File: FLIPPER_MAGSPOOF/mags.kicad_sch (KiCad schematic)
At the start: 7 parts, among them J2 Conn_01x10_Socket, J3 Coil, J3 Conn_01x08_Socket, J4 Conn_01x08_Socket, J5 Conn_01x10_Socket, SW1 On, U3 TC4424

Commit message: BOM updated
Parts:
- J2: LCSC# C492418 -> C57369; manf# PZ254R-11-10P -> (none)
- J3: LCSC# C2894950 -> C492407; manf# PZ254-1-08-W-8.5 -> (none)
- J4: LCSC# C2894950 -> C492407; manf# PZ254-1-08-W-8.5 -> (none); now not fitted
- J5: LCSC# C492418 -> C57369; manf# PZ254R-11-10P -> (none); now not fitted
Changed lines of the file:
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@@
       (effects (font (size 1.27 1.27)) hide)
     )
-    (property "manf#" "PZ254-1-08-W-8.5" (at 116.713 36.068 0)
-      (effects (font (size 1.27 1.27)) hide)
-    )
-    (property "LCSC#" "C2894950" (at 116.713 36.068 0)
+    (property "manf#" "" (at 116.713 36.068 0)
+      (effects (font (size 1.27 1.27)) hide)
+    )
+    (property "LCSC#" "C492407" (at 116.713 36.068 0)
       (effects (font (size 1.27 1.27)) hide)
     )
@@
   )
   (symbol (lib_id "Connector:Conn_01x08_Socket") (at 141.2748 37.3126 0) (unit 1)
-    (in_bom yes) (on_board yes) (dnp no)
+    (in_bom yes) (on_board yes) (dnp yes)
     (property "Reference" "J4" (at 139.3698 26.7716 0)
       (effects (font (size 1.27 1.27)) (justify left))
@@
       (effects (font (size 1.27 1.27)) hide)
     )
-    (property "manf#" "PZ254-1-08-W-8.5" (at 141.2748 37.3126 0)
-      (effects (font (size 1.27 1.27)) hide)
-    )
-    (property "LCSC#" "C2894950" (at 141.2748 37.3126 0)
+    (property "manf#" "" (at 141.2748 37.3126 0)
+      (effects (font (size 1.27 1.27)) hide)
+    )
+    (property "LCSC#" "C492407" (at 141.2748 37.3126 0)
       (effects (font (size 1.27 1.27)) hide)
     )
@@
   )
   (symbol (lib_id "Connector:Conn_01x10_Socket") (at 142.5702 72.2376 0) (unit 1)
-    (in_bom yes) (on_board yes) (dnp no)
+    (in_bom yes) (on_board yes) (dnp yes)
     (property "Reference" "J5" (at 141.4272 60.0456 0)
       (effects (font (size 1.27 1.27)) (justify left))
@@
       (effects (font (size 1.27 1.27)) hide)
     )
-    (property "manf#" "PZ254R-11-10P" (at 142.5702 72.2376 0)
-      (effects (font (size 1.27 1.27)) hide)
-    )
-    (property "LCSC#" "C492418" (at 142.5702 72.2376 0)
+    (property "manf#" "" (at 142.5702 72.2376 0)
+      (effects (font (size 1.27 1.27)) hide)
+    )
+    (property "LCSC#" "C57369" (at 142.5702 72.2376 0)
       (effects (font (size 1.27 1.27)) hide)
     )
@@
       (effects (font (size 1.27 1.27)) hide)
     )
-    (property "manf#" "PZ254R-11-10P" (at 117.602 73.2536 0)
-      (effects (font (size 1.27 1.27)) hide)
-    )
-    (property "LCSC#" "C492418" (at 117.602 73.2536 0)
-      (effects (font (size 1.27 1.27)) hide)
-    )
+    (property "manf#" "" (at 117.602 73.2536 0)
+      (effects (font (size 1.27 1.27)) hide)
+    )
+    (property "LCSC#" "C57369" (at 117.602 73.2536 0)
+      (effects (font (size 1.27 1.27)) hide)
+    )

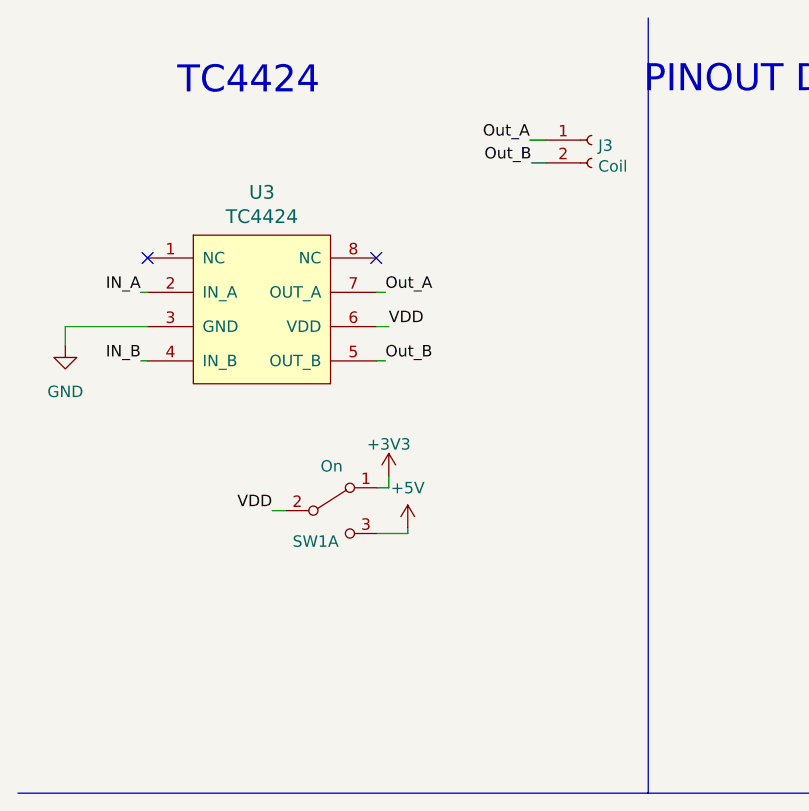
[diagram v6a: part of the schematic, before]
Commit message: feat(Hw): Coil changed
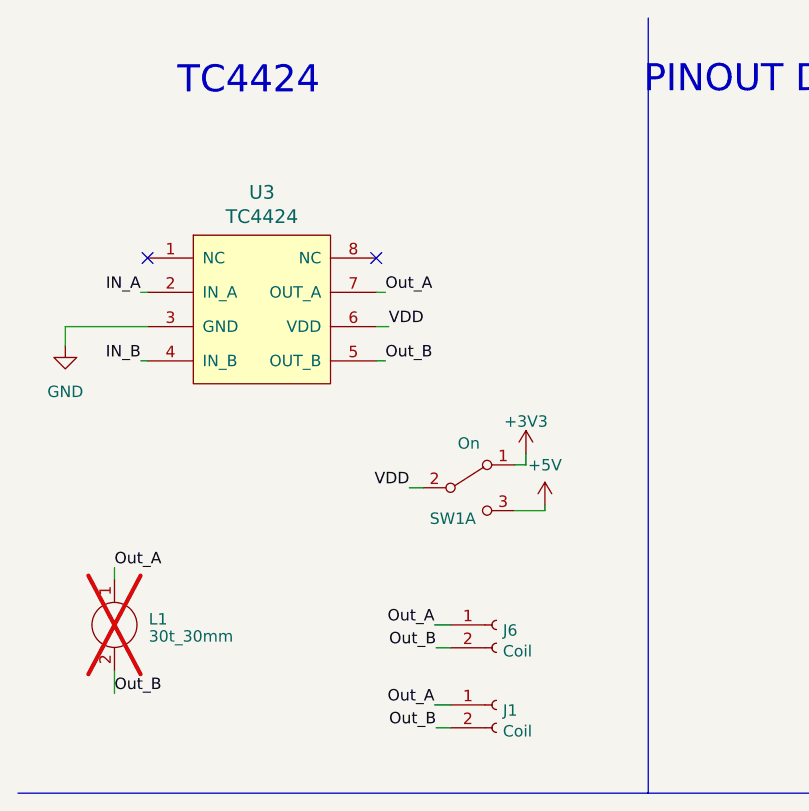
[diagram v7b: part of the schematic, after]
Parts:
- removed J3: Coil, Connector_PinHeader_2.54mm:PinHeader_1x02_P2.54mm_Vertical, symbol Connector:Conn_01x02_Female
- added J1, J6: Coil, Connector_PinHeader_2.54mm:PinHeader_1x02_P2.54mm_Vertical, symbol Connector:Conn_01x02_Female
- added L1: 30t_30mm, Library:Coil_30t_30mm_0.2_0.2_0.6_0.3, symbol Magspoof:Coil_20t_35mm_0.2_0.6_0.3
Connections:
- net Out_A: now also J1.1 (Pin_1), J6.1 (Pin_1), L1.1
- net Out_B: now also J1.2 (Pin_2), J6.2 (Pin_2), L1.2
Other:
- moved on the sheet: SW1A

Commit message: feat(Hw): add capacitor formosfet driver
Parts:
- added C1: 10uF, Capacitor_SMD:C_0603_1608Metric, symbol Device:C
- SW1: LCSC# (none) -> C221660
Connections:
- net GND: now also C1.2
- net VDD: now also C1.1
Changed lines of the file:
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@@
+	(wire
+		(pts
+			(xy 39.37 57.15) (xy 39.37 59.69)
+		)
+		(stroke
+			(width 0)
+			(type default)
+		)
+	)
 	(wire
 		(pts
@@
 		(pts
 			(xy 59.69 87.63) (xy 61.4934 87.63)
+		)
+		(stroke
+			(width 0)
+			(type default)
+		)
+	)
+	(wire
+		(pts
+			(xy 39.37 67.31) (xy 39.37 69.85)
 		)
 		(stroke
@@
 		)
 	)
+	(label "VDD"
+		(at 39.37 57.15 180)
+		(fields_autoplaced yes)
+		(effects
+			(font
+				(size 1.27 1.27)
+			)
+			(justify right bottom)
+		)
+	)
 	(label "PA14"
 		(at 111.7346 65.6336 180)
@@
 			)
 			(justify right bottom)
+		)
+	)
+	(symbol
+		(lib_id "power:GND")
+		(at 39.37 69.85 0)
+		(unit 1)
+		(exclude_from_sim no)
+		(in_bom yes)
+		(on_board yes)
+		(dnp no)
+		(fields_autoplaced yes)
+		(property "Reference" "#PWR011"
+			(at 39.37 76.2 0)
+			(effects
+				(font
+					(size 1.27 1.27)
+				)
+				(hide yes)
+			)
+		)
+		(property "Value" "GND"
+			(at 39.37 74.93 0)
+			(effects
+				(font
+					(size 1.27 1.27)
+				)
+			)
+		)
+		(property "Footprint" ""
+			(at 39.37 69.85 0)
+			(effects
+				(font
+					(size 1.27 1.27)
+				)
+				(hide yes)
+			)
+		)
+		(property "Datasheet" ""
+			(at 39.37 69.85 0)
+			(effects
+				(font
+					(size 1.27 1.27)
+				)
+				(hide yes)
+			)
+		)
+		(property "Description" ""
+			(at 39.37 69.85 0)
+			(effects
+				(font
+					(size 1.27 1.27)
+				)
+				(hide yes)
+			)
+		)
+		(pin "1"
+		)
+		(instances
+			(project "mags"
+				(path "/c000e998-700d-458d-af0b-55d19d346714"
+					(reference "#PWR011")
+					(unit 1)
+				)
+			)
 		)
 	)
@@
 	)
 	(symbol
+		(lib_id "Device:C")
+		(at 39.37 63.5 0)
+		(unit 1)
+		(exclude_from_sim no)
+		(in_bom yes)
+		(on_board yes)
+		(dnp no)
+		(fields_autoplaced yes)
+		(property "Reference" "C1"
+			(at 43.18 62.2299 0)
+			(effects
+				(font
+					(size 1.27 1.27)
+				)
+				(justify left)
+			)
+		)
+		(property "Value" "10uF"
+			(at 43.18 64.7699 0)
+			(effects
+				(font
+					(size 1.27 1.27)
+				)
+				(justify left)
+			)
+		)
+		(property "Footprint" "Capacitor_SMD:C_0603_1608Metric"
+			(at 40.3352 67.31 0)
+			(effects
+				(font
+					(size 1.27 1.27)
+				)
+				(hide yes)
+			)
+		)
+		(property "Datasheet" "~"
+			(at 39.37 63.5 0)
+			(effects
+				(font
+					(size 1.27 1.27)
+				)
+				(hide yes)
+			)
+		)
+		(property "Description" "Unpolarized capacitor"
+			(at 39.37 63.5 0)
+			(effects
+				(font
+					(size 1.27 1.27)
+				)
+				(hide yes)
+			)
+		)
+		(property "LCSC#" "C380314"
+			(at 39.37 63.5 0)
+			(effects
+				(font
+					(size 1.27 1.27)
+				)
+				(hide yes)
+			)
+		)
+		(pin "1"
+		)
+		(pin "2"
+		)
+		(instances
+			(project "mags"
+				(path "/c000e998-700d-458d-af0b-55d19d346714"
+					(reference "C1")
+					(unit 1)
+				)
+			)
+		)
+	)
+	(symbol
 		(lib_id "Switch:SW_DPDT_x2")
 		(at 63.5 63.5 0)
@@
 			)
 		)
-		(property "LCSC#" ""
+		(property "LCSC#" "C221660"
 			(at 63.5 63.5 0)
 			(effects
